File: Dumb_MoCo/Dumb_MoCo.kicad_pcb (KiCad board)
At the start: 2 copper layers, 38.8 x 59.7 mm, 16 parts, among them U1 VNH7070AS

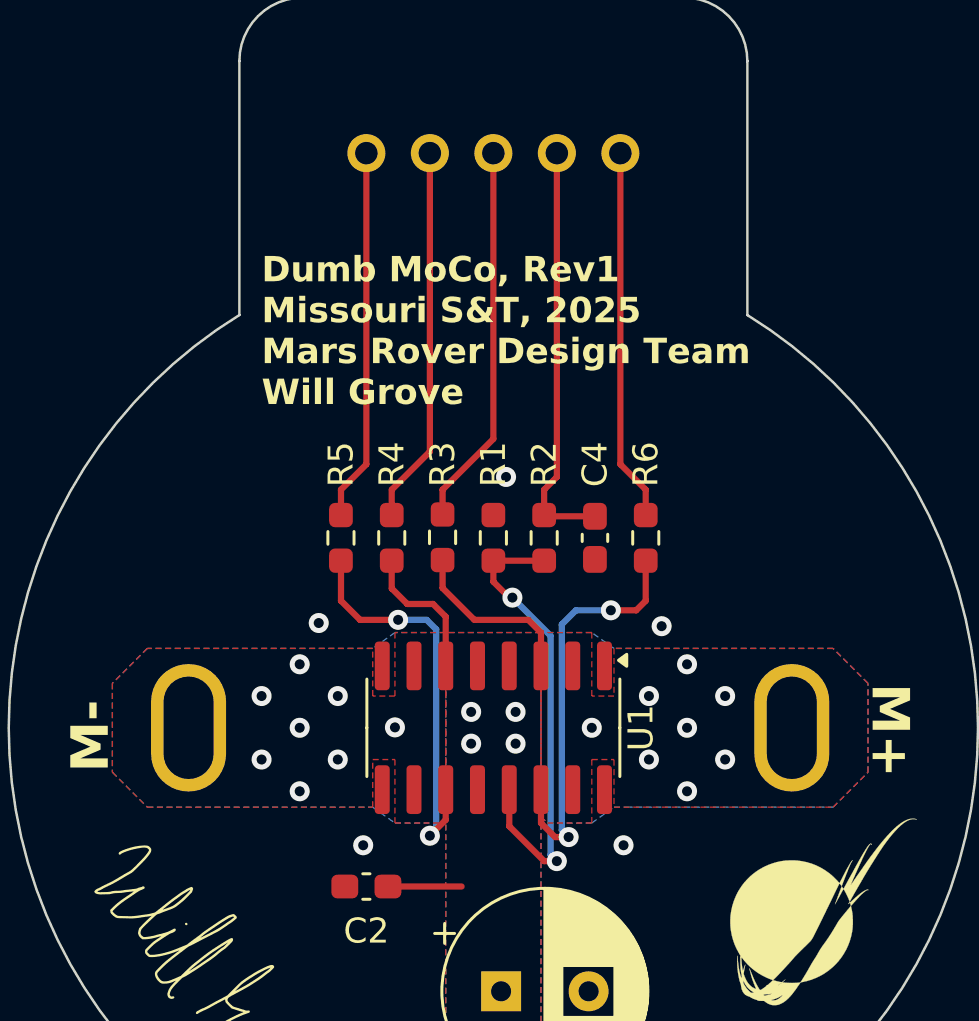
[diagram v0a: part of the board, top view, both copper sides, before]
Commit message: Flipped VNH and reordered SL
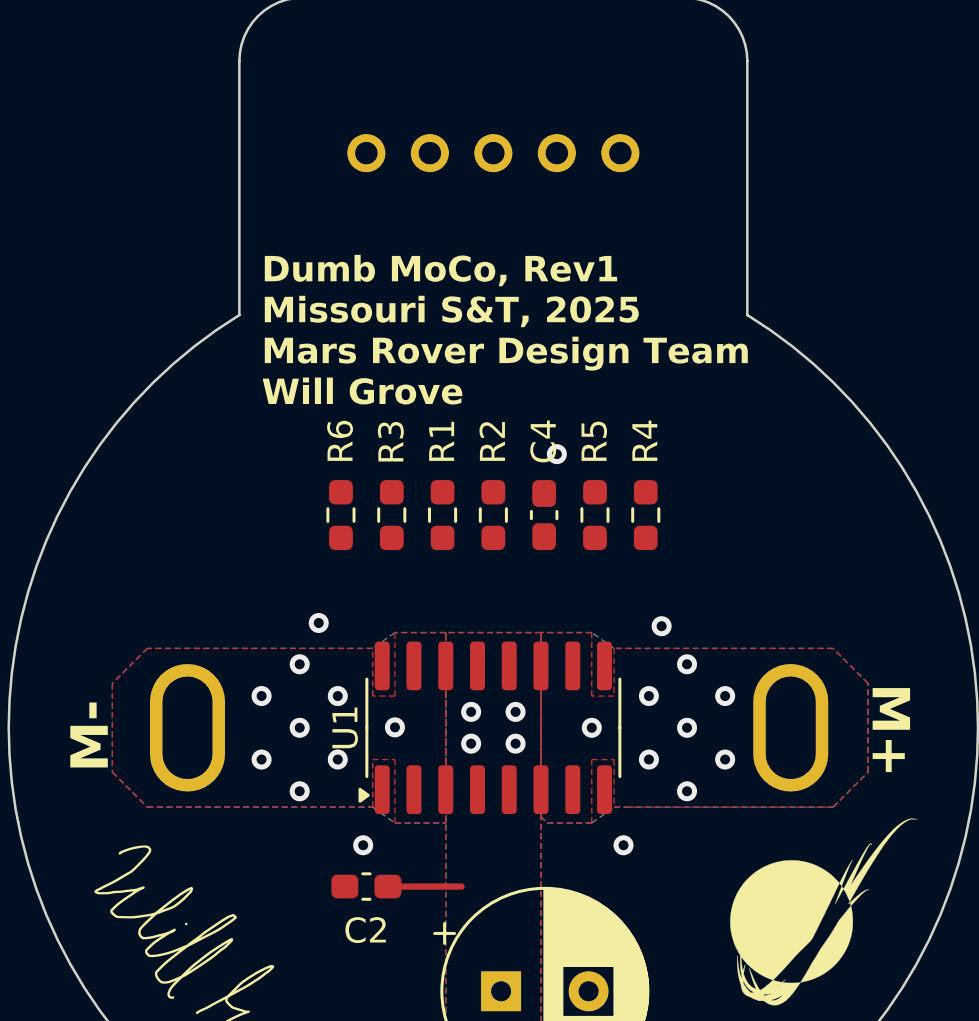
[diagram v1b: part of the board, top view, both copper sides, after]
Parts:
- moved Conn1 24.1 mm to (160.5, 80.0), turned to 180 degrees
- moved R6 12.2 mm to (142.5, 71.5)
- moved R4 10.2 mm to (154.7, 71.5)
- moved R5 10.2 mm to (152.7, 71.5)
- moved R1 2.23 mm to (146.6, 71.5)
- moved R2 2.23 mm to (148.6, 71.5)
- moved C4 2.23 mm to (150.6, 71.5)
- moved R3 2.22 mm to (144.5, 71.5)
- turned U1 to 90 degrees
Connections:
- Conn3 pad 1: SEL -> IN_B
- Conn3 pad 2: CS -> PWM
- Conn3 pad 3: IN_A -> CS
- Conn3 pad 4: IN_B -> IN_A
- Conn3 pad 5: PWM -> SEL
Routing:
- net Net-(U1-CS): track 19.1 -> 0.00 mm, vias 2 -> 0
- net CS: track 16.7 -> 0.00 mm
- net Net-(U1-SEL): track 16.6 -> 0.00 mm, vias 2 -> 0
- net Net-(U1-PWM): track 16.4 -> 0.00 mm, vias 2 -> 0
- net IN_A: track 15.3 -> 0.00 mm
- net IN_B: track 15.1 -> 0.00 mm
- net SEL: track 14.9 -> 0.00 mm
- net PWM: track 14.9 -> 0.00 mm
- net Net-(U1-IN_A): track 7.13 -> 0.00 mm
- net Net-(U1-IN_B): track 5.71 -> 0.00 mm

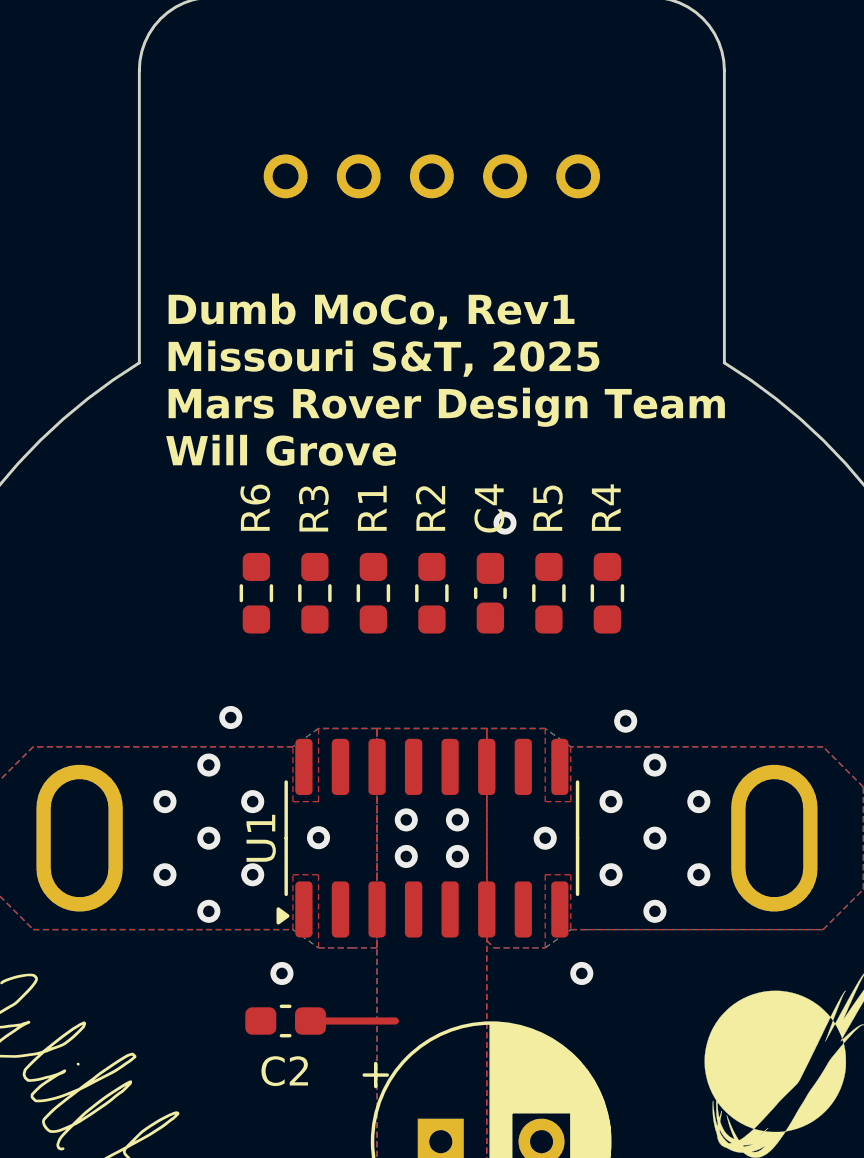
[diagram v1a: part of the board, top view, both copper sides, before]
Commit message: Reordered SL
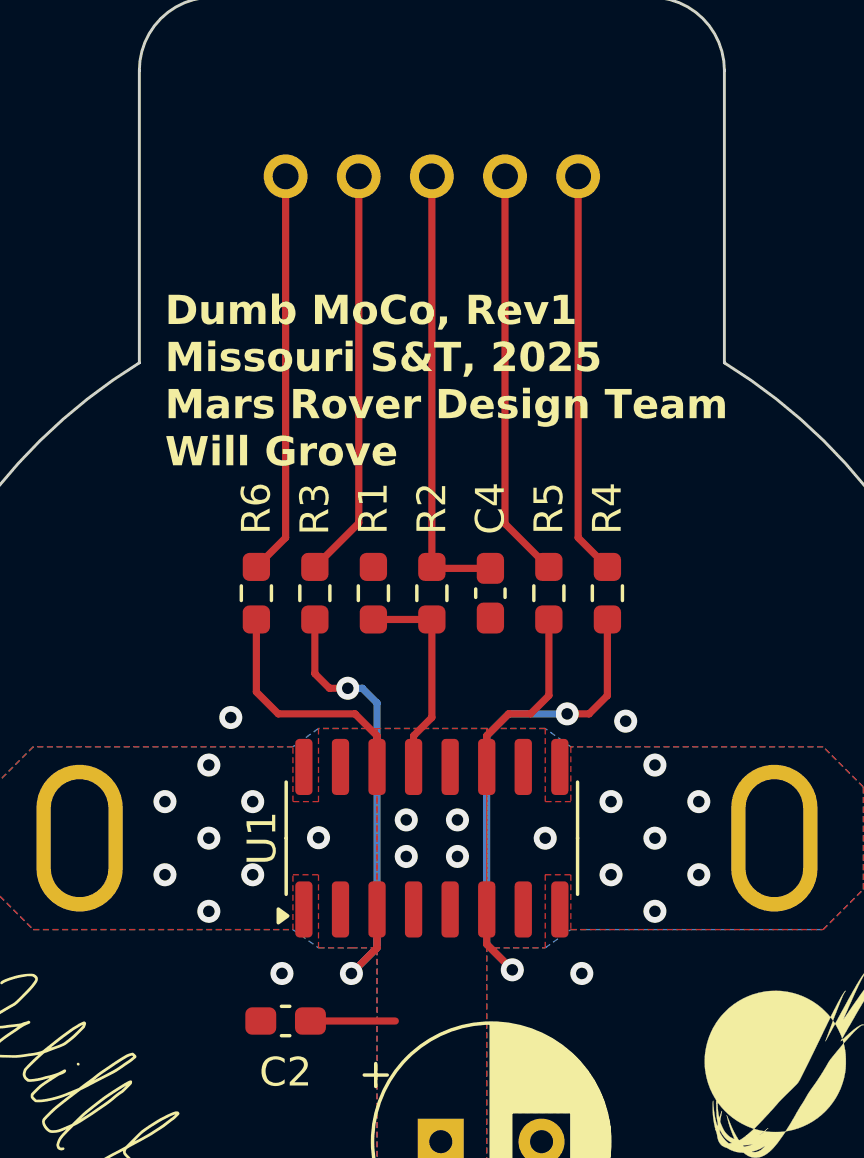
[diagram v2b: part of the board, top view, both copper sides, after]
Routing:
- net Net-(U1-IN_B): track 0.00 -> 18.4 mm, vias 0 -> 2
- net Net-(U1-IN_A): track 0.00 -> 16.8 mm, vias 0 -> 2
- net CS: track 0.00 -> 15.6 mm
- net PWM: track 0.00 -> 14.2 mm
- net IN_A: track 0.00 -> 14.2 mm
- net IN_B: track 0.00 -> 14.0 mm
- net SEL: track 0.00 -> 14.0 mm
- net Net-(U1-SEL): track 0.00 -> 8.42 mm
- net Net-(U1-CS): track 0.00 -> 7.42 mm
- net Net-(U1-PWM): track 0.00 -> 6.46 mm
- net GND: vias 5 -> 4
